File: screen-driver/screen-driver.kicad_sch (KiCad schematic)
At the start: 0 parts

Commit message: added connector footprints and symbols!
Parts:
- added U1: ~, footprints:AXT560124 (socket), symbol AXT_60124:_5_SOCKET
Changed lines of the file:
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@@
 	(generator_version "9.0")
 	(paper "A4")
+	(symbol
+		(lib_id "AXT_60124:_5_SOCKET")
+		(at 59.69 85.09 0)
+		(unit 1)
+		(exclude_from_sim no)
+		(in_bom yes)
+		(on_board yes)
+		(dnp no)
+		(fields_autoplaced yes)
+		(property "Reference" "U1"
+			(at 59.69 107.95 0)
+			(effects
+				(font
+					(size 1.27 1.27)
+				)
+			)
+		)
+		(property "Value" "~"
+			(at 59.69 109.22 0)
+			(effects
+				(font
+					(size 1.27 1.27)
+				)
+			)
+		)
+		(property "Footprint" "footprints:AXT560124 (socket)"
+			(at 59.69 85.09 0)
+			(effects
+				(font
+					(size 1.27 1.27)
+				)
+				(hide yes)
+			)
+		)
+		(property "Datasheet" ""
+			(at 59.69 85.09 0)
+			(effects
+				(font
+					(size 1.27 1.27)
+				)
+				(hide yes)
+			)
+		)
+		(property "Description" ""
+			(at 59.69 85.09 0)
+			(effects
+				(font
+					(size 1.27 1.27)
+				)
+				(hide yes)
+			)
+		)
+		(pin "15"
+		)
+		(pin "19"
+		)
+		(pin "33"
+		)
+		(pin "6"
+		)
+		(pin "2"
+		)
+		(pin "31"
+		)
+		(pin "34"
+		)
+		(pin "18"
+		)
+		(pin "24"
+		)
+		(pin "59"
+		)
+		(pin "40"
+		)
+		(pin "21"
+		)
+		(pin "30"
+		)
+		(pin "13"
+		)
+		(pin "14"
+		)
+		(pin "22"
+		)
+		(pin "52"
+		)
+		(pin "26"
+		)
+		(pin "10"
+		)
+		(pin "5"
+		)
+		(pin "9"
+		)
+		(pin "4"
+		)
+		(pin "50"
+		)
+		(pin "3"
+		)
+		(pin "29"
+		)
+		(pin "41"
+		)
+		(pin "GND"
+		)
+		(pin "32"
+		)
+		(pin "17"
+		)
+		(pin "39"
+		)
+		(pin "16"
+		)
+		(pin "55"
+		)
+		(pin "1"
+		)
+		(pin "44"
+		)
+		(pin "54"
+		)
+		(pin "60"
+		)
+		(pin "28"
+		)
+		(pin "7"
+		)
+		(pin "23"
+		)
+		(pin "43"
+		)
+		(pin "48"
+		)
+		(pin "8"
+		)
+		(pin "58"
+		)
+		(pin "11"
+		)
+		(pin "20"
+		)
+		(pin "46"
+		)
+		(pin "51"
+		)
+		(pin "38"
+		)
+		(pin "45"
+		)
+		(pin "35"
+		)
+		(pin "56"
+		)
+		(pin "49"
+		)
+		(pin "47"
+		)
+		(pin "57"
+		)
+		(pin "25"
+		)
+		(pin "42"
+		)
+		(pin "37"
+		)
+		(pin "12"
+		)
+		(pin "27"
+		)
+		(pin "36"
+		)
+		(pin "53"
+		)
+		(instances
+			(project ""
+				(path "/cb3fd18d-9eb3-49d0-830e-3b5c4c92488c"
+					(reference "U1")
+					(unit 1)
+				)
+			)
+		)
+	)
 	(sheet_instances
 		(path "/"

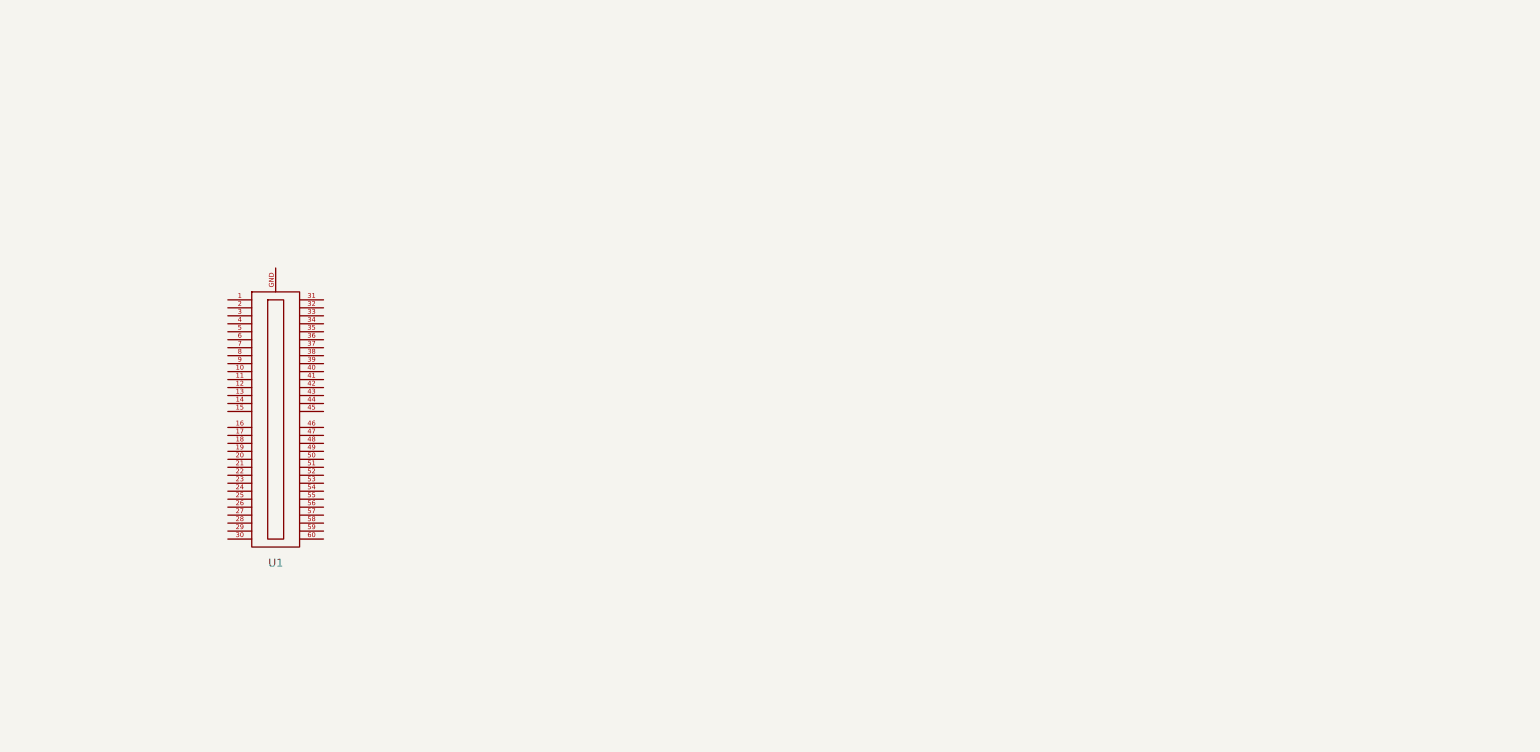
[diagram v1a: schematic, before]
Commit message: footprints + had to change the eDP to LVDS IC for a 4 channel one
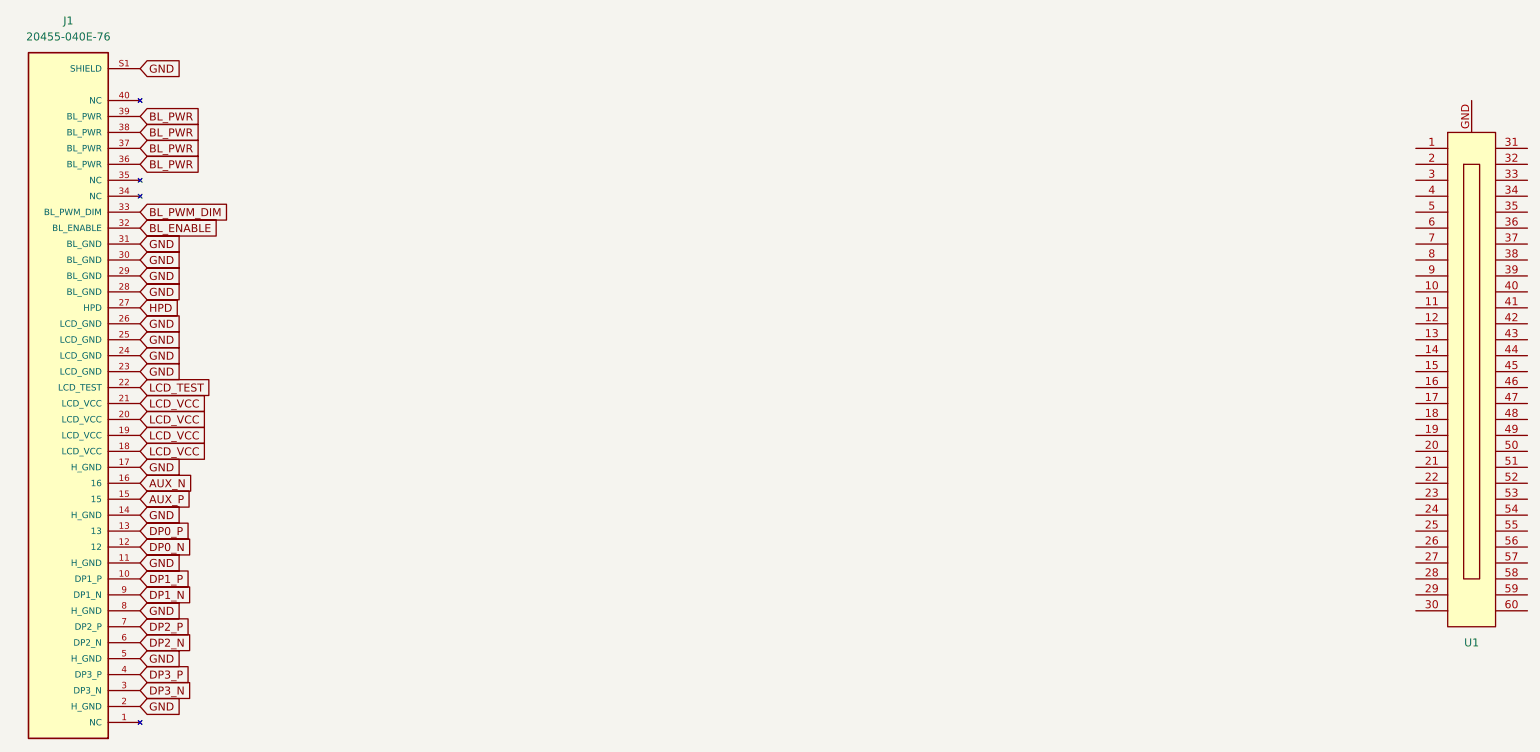
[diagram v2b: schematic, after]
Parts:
- added J1: 20455-040E-76, footprints:IPEX_20455-040E-76, symbol 20455-040E-76:20455-040E-76_screen_BOE-NE135FBM-N41
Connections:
- new net AUX_N: J1.16
- new net AUX_P: J1.15
- new net BL_ENABLE: J1.32 (BL_ENABLE)
- new net BL_PWM_DIM: J1.33 (BL_PWM_DIM)
- new net BL_PWR: J1.36 (BL_PWR), J1.37 (BL_PWR), J1.38 (BL_PWR), J1.39 (BL_PWR)
- new net DP0_N: J1.12
- new net DP0_P: J1.13
- new net DP1_N: J1.9 (DP1_N)
- new net DP1_P: J1.10 (DP1_P)
- new net DP2_N: J1.6 (DP2_N)
- new net DP2_P: J1.7 (DP2_P)
- new net DP3_N: J1.3 (DP3_N)
- new net DP3_P: J1.4 (DP3_P)
- new net GND: J1.11 (H_GND), J1.14 (H_GND), J1.17 (H_GND), J1.2 (H_GND), J1.23 (LCD_GND), J1.24 (LCD_GND), J1.25 (LCD_GND), J1.26 (LCD_GND), J1.28 (BL_GND), J1.29 (BL_GND), J1.30 (BL_GND), J1.31 (BL_GND), J1.5 (H_GND), J1.8 (H_GND), J1.S1 (SHIELD), J1.S2 (SHIELD), J1.S3 (SHIELD), J1.S4 (SHIELD)
- new net HPD: J1.27 (HPD)
- new net LCD_TEST: J1.22 (LCD_TEST)
- new net LCD_VCC: J1.18 (LCD_VCC), J1.19 (LCD_VCC), J1.20 (LCD_VCC), J1.21 (LCD_VCC)
